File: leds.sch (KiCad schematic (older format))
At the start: 34 parts, among them U5 PCA9635

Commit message: Update LED models, footprints, schematic, and PCB.
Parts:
- removed C10, C12, C15: 10u, Capacitor_SMD:C_0805_2012Metric, symbol Drone:CAP
- removed C11, C13, C9: 100n, Capacitor_SMD:C_0805_2012Metric, symbol Drone:CAP
- removed D? (x4): LED (R), Drone:C503B, symbol Drone:LED
- removed D? (x4): LED (G), Drone:C503B, symbol Drone:LED
- removed D? (x4): LED (B), Drone:C503B, symbol Drone:LED
- removed R20, R23, R26: 210, Resistor_SMD:R_0805_2012Metric, symbol Drone:RES
- removed R21, R24, R27: 250, Resistor_SMD:R_0805_2012Metric, symbol Drone:RES
- removed R22, R25, R28: 290, Resistor_SMD:R_0805_2012Metric, symbol Drone:RES
- added C? (x3): 10u, Capacitor_SMD:C_0805_2012Metric, symbol Drone:CAP
- added C? (x3): 100n, Capacitor_SMD:C_0805_2012Metric, symbol Drone:CAP
- added D? (x4): LED-RED, Drone:C503B, symbol Drone:LED-RED
- added D? (x4): LED-GREEN, Drone:C503B, symbol Drone:LED-GREEN
- added D? (x4): LED-BLUE, Drone:C503B, symbol Drone:LED-BLUE
- added R? (x6): 100, Resistor_SMD:R_0805_2012Metric, symbol Drone:RES
- added R? (x3): 145, Resistor_SMD:R_0805_2012Metric, symbol Drone:RES
- R?: renamed from R18; value 250 -> 100
- R?: renamed from R17; value 210 -> 100
- R?: renamed from R19; value 290 -> 145
- renumbered C8 to C?, C7 to C?
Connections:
- wire segments 128 -> 124
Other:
- moved on the sheet: C?, R?

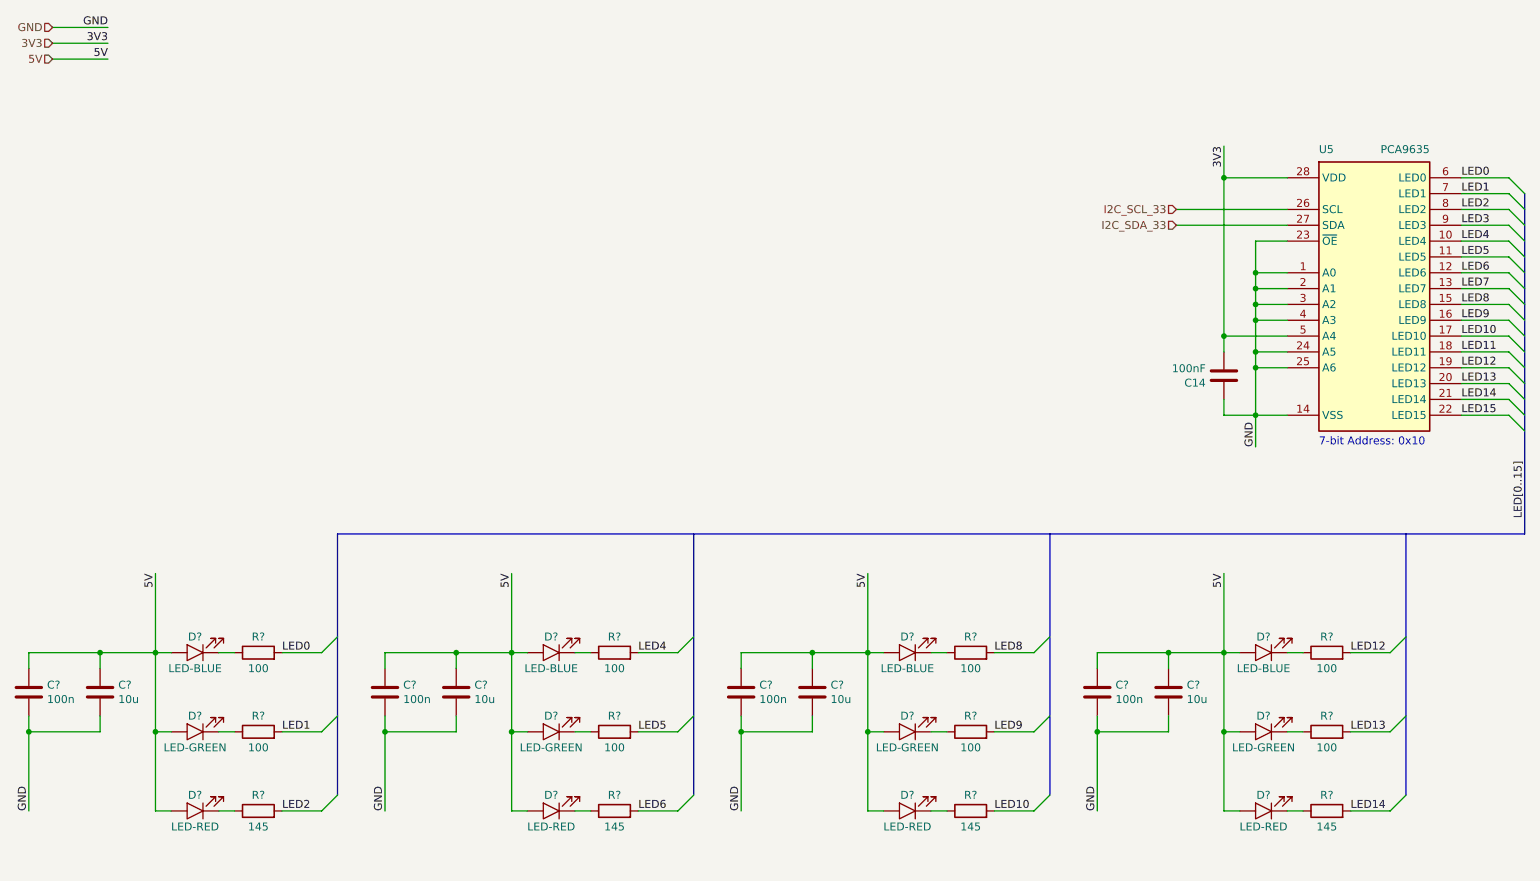
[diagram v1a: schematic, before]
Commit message: Work in progress commit: some duplicate components in PCB.
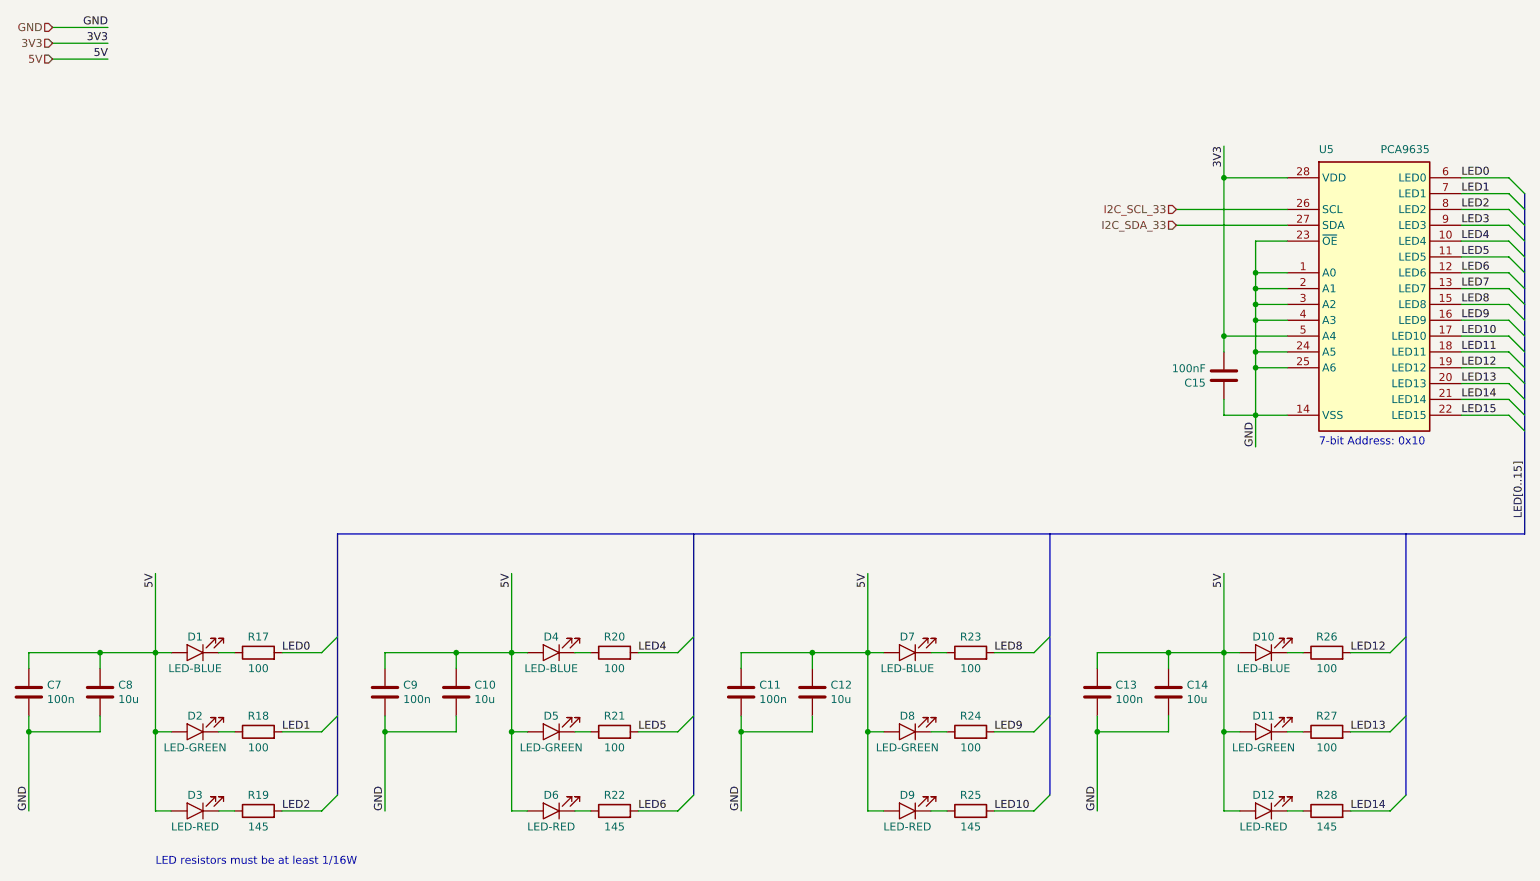
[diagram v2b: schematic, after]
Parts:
- gave numbers to parts that had none: 32
- renumbered C14 to C15
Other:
- note added: "LED resistors must be at least 1/16W"

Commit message: Work in progress on laying out the board.
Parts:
- C10, C11, C12, C13, C14, C15, C7, C8, C9: footprint Capacitor_SMD:C_0805_2012Metric -> Drone:C0805
- R17, R18, R20, R21, R23, R24, R26, R27: footprint Resistor_SMD:R_0805_2012Metric -> Drone:R0805
- R19, R22, R25, R28: value 145 -> 147; footprint Resistor_SMD:R_0805_2012Metric -> Drone:R0805
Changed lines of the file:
@@
 F 0 "R17" V 2600 5000 50  0000 C CNN
 F 1 "100" V 2400 5000 50  0000 C CNN
-F 2 "Resistor_SMD:R_0805_2012Metric" V 2430 5000 50  0001 C CNN
+F 2 "Drone:R0805" V 2430 5000 50  0001 C CNN
 F 3 "~" H 2500 5000 50  0001 C CNN
 	1    2500 5000
@@
 F 0 "R18" V 2600 5500 50  0000 C CNN
 F 1 "100" V 2400 5500 50  0000 C CNN
-F 2 "Resistor_SMD:R_0805_2012Metric" V 2430 5500 50  0001 C CNN
+F 2 "Drone:R0805" V 2430 5500 50  0001 C CNN
 F 3 "~" H 2500 5500 50  0001 C CNN
 	1    2500 5500
@@
 F 0 "C8" H 1615 5296 50  0000 L CNN
 F 1 "10u" H 1615 5205 50  0000 L CNN
-F 2 "Capacitor_SMD:C_0805_2012Metric" H 1538 5100 50  0001 C CNN
+F 2 "Drone:C0805" H 1538 5100 50  0001 C CNN
 F 3 "~" H 1500 5250 50  0001 C CNN
 	1    1500 5250
@@
 F 0 "C7" H 1165 5296 50  0000 L CNN
 F 1 "100n" H 1165 5205 50  0000 L CNN
-F 2 "Capacitor_SMD:C_0805_2012Metric" H 1088 5100 50  0001 C CNN
+F 2 "Drone:C0805" H 1088 5100 50  0001 C CNN
 F 3 "~" H 1050 5250 50  0001 C CNN
 	1    1050 5250
@@
 AR Path="/5E30BD8E/5E39412E" Ref="R19"  Part="1"
 F 0 "R19" V 2600 6000 50  0000 C CNN
-F 1 "145" V 2400 6000 50  0000 C CNN
-F 2 "Resistor_SMD:R_0805_2012Metric" V 2430 6000 50  0001 C CNN
+F 1 "147" V 2400 6000 50  0000 C CNN
+F 2 "Drone:R0805" V 2430 6000 50  0001 C CNN
 F 3 "~" H 2500 6000 50  0001 C CNN
 	1    2500 6000
@@
 F 0 "R20" V 4850 5000 50  0000 C CNN
 F 1 "100" V 4650 5000 50  0000 C CNN
-F 2 "Resistor_SMD:R_0805_2012Metric" V 4680 5000 50  0001 C CNN
+F 2 "Drone:R0805" V 4680 5000 50  0001 C CNN
 F 3 "~" H 4750 5000 50  0001 C CNN
 	1    4750 5000
@@
 F 0 "R21" V 4850 5500 50  0000 C CNN
 F 1 "100" V 4650 5500 50  0000 C CNN
-F 2 "Resistor_SMD:R_0805_2012Metric" V 4680 5500 50  0001 C CNN
+F 2 "Drone:R0805" V 4680 5500 50  0001 C CNN
 F 3 "~" H 4750 5500 50  0001 C CNN
 	1    4750 5500
@@
 F 0 "C10" H 3865 5296 50  0000 L CNN
 F 1 "10u" H 3865 5205 50  0000 L CNN
-F 2 "Capacitor_SMD:C_0805_2012Metric" H 3788 5100 50  0001 C CNN
+F 2 "Drone:C0805" H 3788 5100 50  0001 C CNN
 F 3 "~" H 3750 5250 50  0001 C CNN
 	1    3750 5250
@@
 F 0 "C9" H 3415 5296 50  0000 L CNN
 F 1 "100n" H 3415 5205 50  0000 L CNN
-F 2 "Capacitor_SMD:C_0805_2012Metric" H 3338 5100 50  0001 C CNN
+F 2 "Drone:C0805" H 3338 5100 50  0001 C CNN
 F 3 "~" H 3300 5250 50  0001 C CNN
 	1    3300 5250
@@
 AR Path="/5E30BD8E/5E68B73C" Ref="R22"  Part="1"
 F 0 "R22" V 4850 6000 50  0000 C CNN
-F 1 "145" V 4650 6000 50  0000 C CNN
-F 2 "Resistor_SMD:R_0805_2012Metric" V 4680 6000 50  0001 C CNN
+F 1 "147" V 4650 6000 50  0000 C CNN
+F 2 "Drone:R0805" V 4680 6000 50  0001 C CNN
 F 3 "~" H 4750 6000 50  0001 C CNN
 	1    4750 6000
@@
 F 0 "R23" V 7100 5000 50  0000 C CNN
 F 1 "100" V 6900 5000 50  0000 C CNN
-F 2 "Resistor_SMD:R_0805_2012Metric" V 6930 5000 50  0001 C CNN
+F 2 "Drone:R0805" V 6930 5000 50  0001 C CNN
 F 3 "~" H 7000 5000 50  0001 C CNN
 	1    7000 5000
@@
 F 0 "R24" V 7100 5500 50  0000 C CNN
 F 1 "100" V 6900 5500 50  0000 C CNN
-F 2 "Resistor_SMD:R_0805_2012Metric" V 6930 5500 50  0001 C CNN
+F 2 "Drone:R0805" V 6930 5500 50  0001 C CNN
 F 3 "~" H 7000 5500 50  0001 C CNN
 	1    7000 5500
@@
 F 0 "C12" H 6115 5296 50  0000 L CNN
 F 1 "10u" H 6115 5205 50  0000 L CNN
-F 2 "Capacitor_SMD:C_0805_2012Metric" H 6038 5100 50  0001 C CNN
+F 2 "Drone:C0805" H 6038 5100 50  0001 C CNN
 F 3 "~" H 6000 5250 50  0001 C CNN
 	1    6000 5250
@@
 F 0 "C11" H 5665 5296 50  0000 L CNN
 F 1 "100n" H 5665 5205 50  0000 L CNN
-F 2 "Capacitor_SMD:C_0805_2012Metric" H 5588 5100 50  0001 C CNN
+F 2 "Drone:C0805" H 5588 5100 50  0001 C CNN
 F 3 "~" H 5550 5250 50  0001 C CNN
 	1    5550 5250
@@
 AR Path="/5E30BD8E/5E68FFB1" Ref="R25"  Part="1"
 F 0 "R25" V 7100 6000 50  0000 C CNN
-F 1 "145" V 6900 6000 50  0000 C CNN
-F 2 "Resistor_SMD:R_0805_2012Metric" V 6930 6000 50  0001 C CNN
+F 1 "147" V 6900 6000 50  0000 C CNN
+F 2 "Drone:R0805" V 6930 6000 50  0001 C CNN
 F 3 "~" H 7000 6000 50  0001 C CNN
 	1    7000 6000
@@
 F 0 "R26" V 9350 5000 50  0000 C CNN
 F 1 "100" V 9150 5000 50  0000 C CNN
-F 2 "Resistor_SMD:R_0805_2012Metric" V 9180 5000 50  0001 C CNN
+F 2 "Drone:R0805" V 9180 5000 50  0001 C CNN
 F 3 "~" H 9250 5000 50  0001 C CNN
 	1    9250 5000
@@
 F 0 "R27" V 9350 5500 50  0000 C CNN
 F 1 "100" V 9150 5500 50  0000 C CNN
-F 2 "Resistor_SMD:R_0805_2012Metric" V 9180 5500 50  0001 C CNN
+F 2 "Drone:R0805" V 9180 5500 50  0001 C CNN
 F 3 "~" H 9250 5500 50  0001 C CNN
 	1    9250 5500
@@
 F 0 "C14" H 8365 5296 50  0000 L CNN
 F 1 "10u" H 8365 5205 50  0000 L CNN
-F 2 "Capacitor_SMD:C_0805_2012Metric" H 8288 5100 50  0001 C CNN
+F 2 "Drone:C0805" H 8288 5100 50  0001 C CNN
 F 3 "~" H 8250 5250 50  0001 C CNN
 	1    8250 5250
@@
 F 0 "C13" H 7915 5296 50  0000 L CNN
 F 1 "100n" H 7915 5205 50  0000 L CNN
-F 2 "Capacitor_SMD:C_0805_2012Metric" H 7838 5100 50  0001 C CNN
+F 2 "Drone:C0805" H 7838 5100 50  0001 C CNN
 F 3 "~" H 7800 5250 50  0001 C CNN
 	1    7800 5250
@@
 AR Path="/5E30BD8E/5E696D3C" Ref="R28"  Part="1"
 F 0 "R28" V 9350 6000 50  0000 C CNN
-F 1 "145" V 9150 6000 50  0000 C CNN
-F 2 "Resistor_SMD:R_0805_2012Metric" V 9180 6000 50  0001 C CNN
+F 1 "147" V 9150 6000 50  0000 C CNN
+F 2 "Drone:R0805" V 9180 6000 50  0001 C CNN
 F 3 "~" H 9250 6000 50  0001 C CNN
 	1    9250 6000
@@
 F 0 "C15" H 8715 3296 50  0000 L CNN
 F 1 "100nF" H 8715 3205 50  0000 L CNN
-F 2 "Capacitor_SMD:C_0805_2012Metric" H 8638 3100 50  0001 C CNN
+F 2 "Drone:C0805" H 8638 3100 50  0001 C CNN
 F 3 "~" H 8600 3250 50  0001 C CNN
 	1    8600 3250

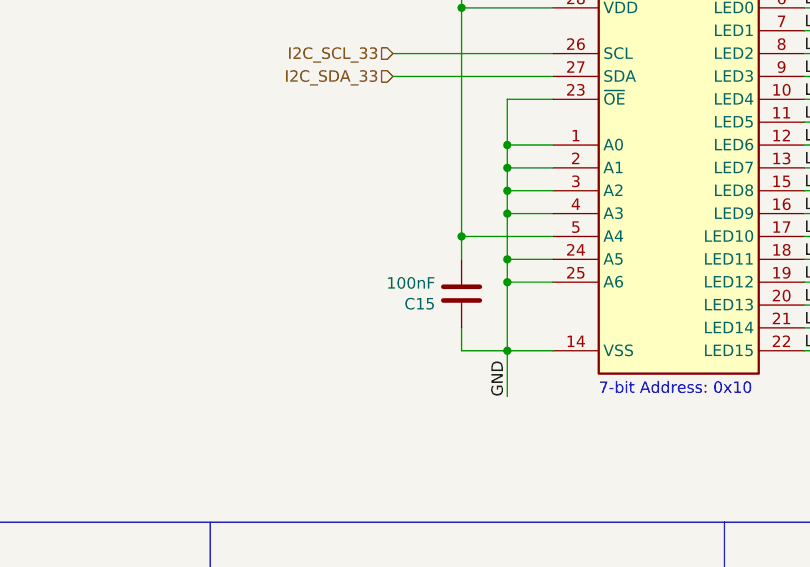
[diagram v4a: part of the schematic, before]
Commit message: minor fix 100cf -> 100n
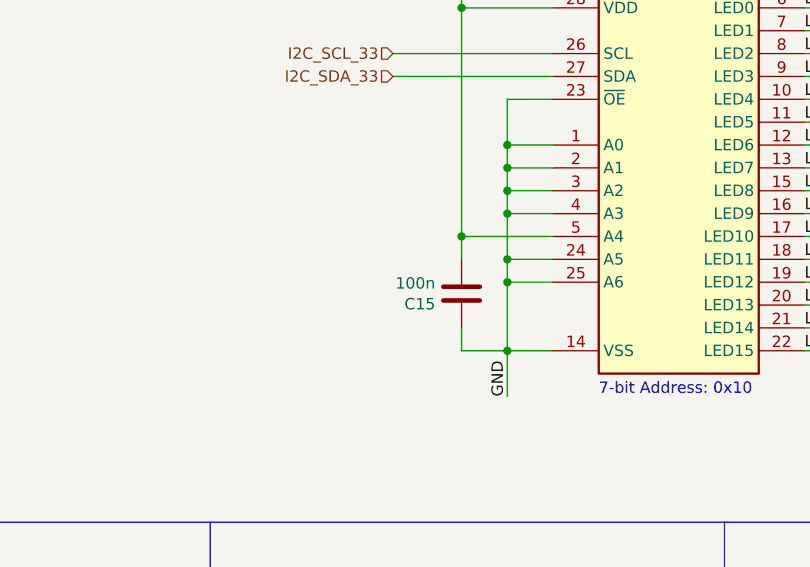
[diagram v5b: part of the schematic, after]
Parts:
- C15: value 100nF -> 100n
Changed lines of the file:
@@
 AR Path="/5E30BD8E/5E322DC6" Ref="C15"  Part="1"
 F 0 "C15" H 8715 3296 50  0000 L CNN
-F 1 "100nF" H 8715 3205 50  0000 L CNN
+F 1 "100n" H 8715 3205 50  0000 L CNN
 F 2 "Drone:C0805" H 8638 3100 50  0001 C CNN
 F 3 "~" H 8600 3250 50  0001 C CNN

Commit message: Update layout
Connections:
- net LED11: no longer names the net of U5.18 (LED11)
- net LED15: no longer names the net of U5.22 (LED15)
- net LED3: no longer names the net of U5.9 (LED3)
- net LED7: no longer names the net of U5.13 (LED7)
- no-connect marks 0 -> 4
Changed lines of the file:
@@
 	0    -1   -1   0
 $EndComp
-Text Label 10100 3500 0    50   ~ 0
-LED15
 Text Label 10100 3400 0    50   ~ 0
 LED14
@@
 Text Label 10100 3200 0    50   ~ 0
 LED12
-Text Label 10100 3100 0    50   ~ 0
-LED11
 Text Label 10100 3000 0    50   ~ 0
 LED10
@@
 Text Label 10100 2800 0    50   ~ 0
 LED8
-Text Label 10100 2700 0    50   ~ 0
-LED7
 Text Label 10100 2600 0    50   ~ 0
 LED6
@@
 Text Label 10100 2400 0    50   ~ 0
 LED4
-Text Label 10100 2300 0    50   ~ 0
-LED3
 Text Label 10100 2200 0    50   ~ 0
 LED2
@@
 LED0
 Wire Wire Line
-	10100 3500 10400 3500
-Wire Wire Line
 	10100 3400 10400 3400
 Wire Wire Line
@@
 LED[0..15]
 Entry Wire Line
-	10400 3500 10500 3600
-Entry Wire Line
 	10400 3400 10500 3500
 Entry Wire Line
@@
 	10400 3200 10500 3300
 Entry Wire Line
-	10400 3100 10500 3200
-Entry Wire Line
 	10400 3000 10500 3100
 Entry Wire Line
@@
 	10400 2800 10500 2900
 Entry Wire Line
-	10400 2700 10500 2800
-Entry Wire Line
 	10400 2600 10500 2700
 Entry Wire Line
@@
 Entry Wire Line
 	10400 2400 10500 2500
-Entry Wire Line
-	10400 2300 10500 2400
 Entry Wire Line
 	10400 2200 10500 2300
@@
 	10100 3200 10400 3200
 Wire Wire Line
-	10100 3100 10400 3100
-Wire Wire Line
 	10100 3000 10400 3000
 Wire Wire Line
@@
 	10100 2800 10400 2800
 Wire Wire Line
-	10100 2700 10400 2700
-Wire Wire Line
 	10100 2600 10400 2600
 Wire Wire Line
@@
 Wire Wire Line
 	10100 2400 10400 2400
-Wire Wire Line
-	10100 2300 10400 2300
 Wire Wire Line
 	10100 2200 10400 2200
@@
 	-1   0    0    1
 $EndComp
+NoConn ~ 10100 2300
+NoConn ~ 10100 2700
+NoConn ~ 10100 3100
+NoConn ~ 10100 3500
 Wire Bus Line
 	3000 4250 3000 5900

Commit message: Placement complete.
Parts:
- removed U5: PCA9635, Package_SO:TSSOP-28_4.4x9.7mm_P0.65mm, symbol Drone:PCA9635
- added U5: PCA9635PW, Drone:PCA9635PW, symbol Drone:PCA9635PW
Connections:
- net 3V3: now also U5.28 (VDD), U5.5 (A4)
- net GND: now also U5.1 (A0), U5.14 (VSS), U5.2 (A1), U5.23 (~OE), U5.24 (A5), U5.25 (A6), U5.3 (A2), U5.4 (A3)
- net I2C_SCL_33: now also U5.26 (SCL)
- net I2C_SDA_33: now also U5.27 (SDA)
- net LED0: now also U5.6 (LED0)
- net LED1: now also U5.7 (LED1)
- net LED10: now also U5.17 (LED10)
- net LED12: now also U5.19 (LED12)
- net LED13: now also U5.20 (LED13)
- net LED14: now also U5.21 (LED14)
- net LED2: now also U5.8 (LED2)
- net LED4: now also U5.10 (LED4)
- net LED5: now also U5.11 (LED5)
- net LED6: now also U5.12 (LED6)
- net LED8: now also U5.15 (LED8)
- net LED9: now also U5.16 (LED9)
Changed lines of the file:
@@
 Wire Wire Line
 	10100 2200 10400 2200
-$Comp
-L Drone:PCA9635 U5
-U 1 1 5E31FD58
-P 9550 1900
-F 0 "U5" H 9200 1950 50  0000 L BNN
-F 1 "PCA9635" H 9900 1950 50  0000 R BNN
-F 2 "Package_SO:TSSOP-28_4.4x9.7mm_P0.65mm" H 9200 2150 50  0001 L BNN
-F 3 "" H 9550 1000 50  0001 C CNN
-	1    9550 1900
-	1    0    0    -1
-$EndComp
 Wire Wire Line
 	8800 2400 8800 2600
@@
 Wire Bus Line
 	10500 2100 10500 4250
+$Comp
+L Drone:PCA9635PW U5
+U 1 1 5E9D9194
+P 9550 1900
+F 0 "U5" H 9550 2067 50  0000 C CNN
+F 1 "PCA9635PW" H 9550 1950 50  0000 C CNN
+F 2 "Drone:PCA9635PW" H 9200 2150 50  0001 L BNN
+F 3 "" H 9550 1000 50  0001 C CNN
+	1    9550 1900
+	1    0    0    -1
+$EndComp
 $EndSCHEMATC
